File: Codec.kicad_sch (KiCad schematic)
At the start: 1 part, among them U5 TAC5242

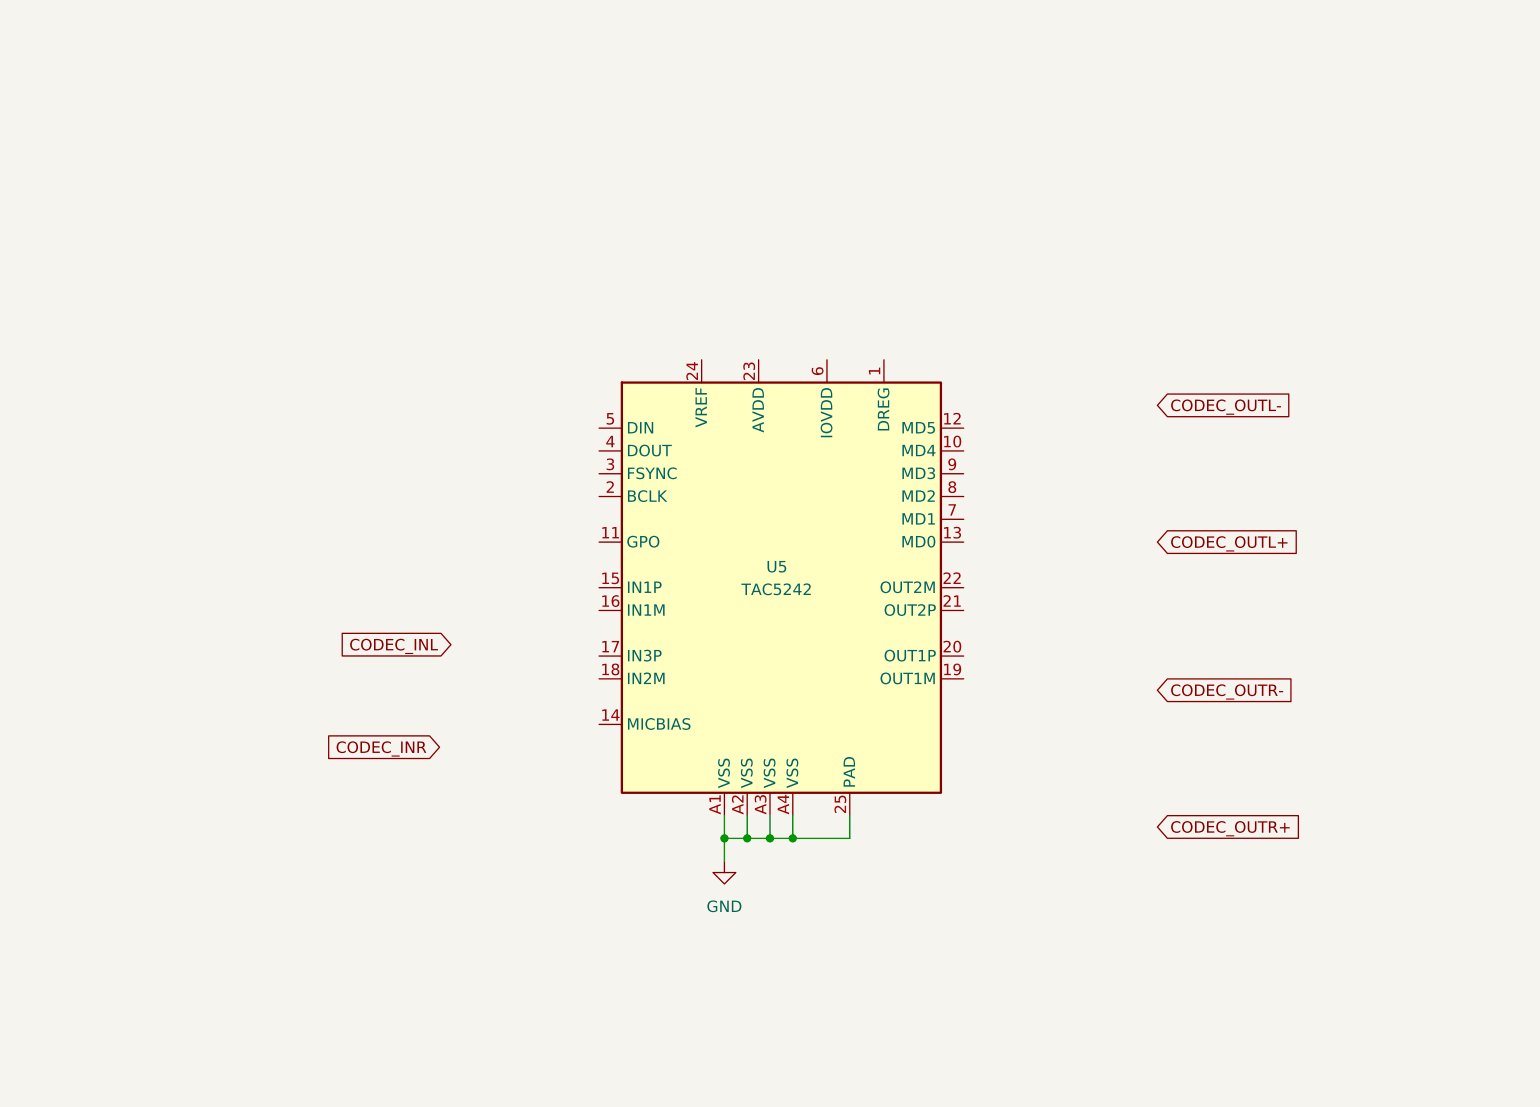
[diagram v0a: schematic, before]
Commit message: Schematic
Updated the schematic.
Added the codec schematic module.
Added the buffer schematic module.
Added the RP2350 schematic module.
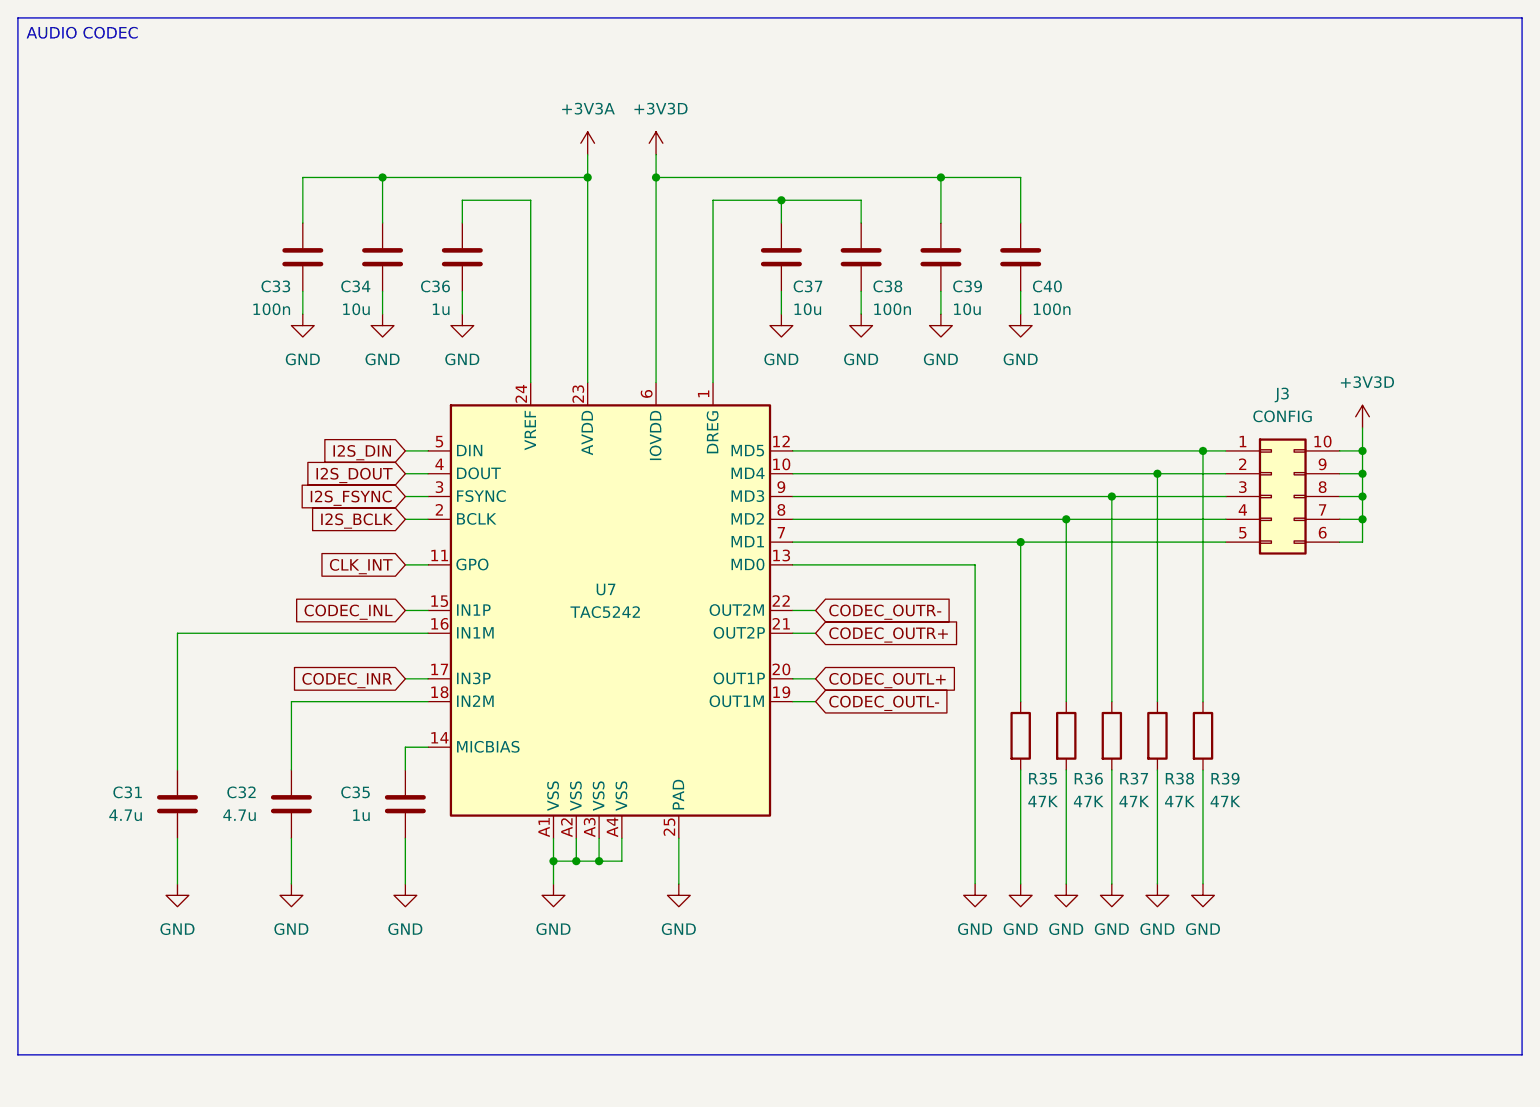
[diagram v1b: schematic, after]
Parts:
- added C31, C32: 4.7u, Capacitor_SMD:C_1206_3216Metric, symbol Device:C
- added C33, C38, C40: 100n, Capacitor_SMD:C_0603_1608Metric, symbol Device:C
- added C34, C37, C39: 10u, Capacitor_SMD:C_1206_3216Metric, symbol Device:C
- added C35, C36: 1u, Capacitor_SMD:C_0805_2012Metric, symbol Device:C
- added J3: CONFIG, Connector_PinHeader_1.27mm:PinHeader_2x05_P1.27mm_Vertical, symbol Connector_Generic:Conn_02x05_Counter_Clockwise
- added R35, R36, R37, R38, R39: 47K, Resistor_SMD:R_0603_1608Metric, symbol Device:R
- renumbered U5 to U7
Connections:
- net CODEC_INL: now also U7.15 (IN1P)
- net CODEC_INR: now also U7.17 (IN3P)
- net CODEC_OUTL+: now also U7.20 (OUT1P)
- net CODEC_OUTL-: now also U7.19 (OUT1M)
- net CODEC_OUTR+: now also U7.21 (OUT2P)
- net CODEC_OUTR-: now also U7.22 (OUT2M)
- net GND: now also U7.13 (MD0), C31.2, C32.2, C33.2, C34.2, C35.2, C36.2, C37.2, C38.2, C39.2, C40.2, R35.2, R36.2, R37.2, R38.2, R39.2
- net at U7.1 (DREG): now also C37.1, C38.1
- net at U7.10 (MD4): now also J3.2 (Pin_2), R38.1
- net CLK_INT: now reaches U7.11 (GPO)
- net at U7.12 (MD5): now also J3.1 (Pin_1), R39.1
- net at U7.14 (MICBIAS): now also C35.1
- net at U7.16 (IN1M): now also C31.1
- net at U7.18 (IN2M): now also C32.1
- net I2S_BCLK: now reaches U7.2 (BCLK)
- net +3V3A: now reaches U7.23 (AVDD)
- net +3V3A: now also C33.1, C34.1
- net at U7.24 (VREF): now also C36.1
- net I2S_FSYNC: now reaches U7.3 (FSYNC)
- net I2S_DOUT: now reaches U7.4 (DOUT)
- net I2S_DIN: now reaches U7.5 (DIN)
- net +3V3D: now reaches U7.6 (IOVDD)
- net +3V3D: now also C39.1, C40.1, J3.10 (Pin_10), J3.6 (Pin_6), J3.7 (Pin_7), J3.8 (Pin_8), J3.9 (Pin_9)
- net at U7.7 (MD1): now also J3.5 (Pin_5), R35.1
- net at U7.8 (MD2): now also J3.4 (Pin_4), R36.1
- net at U7.9 (MD3): now also J3.3 (Pin_3), R37.1
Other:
- moved on the sheet: U7

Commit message: Schematic
Updated the power delivery module.
Other minor changes.
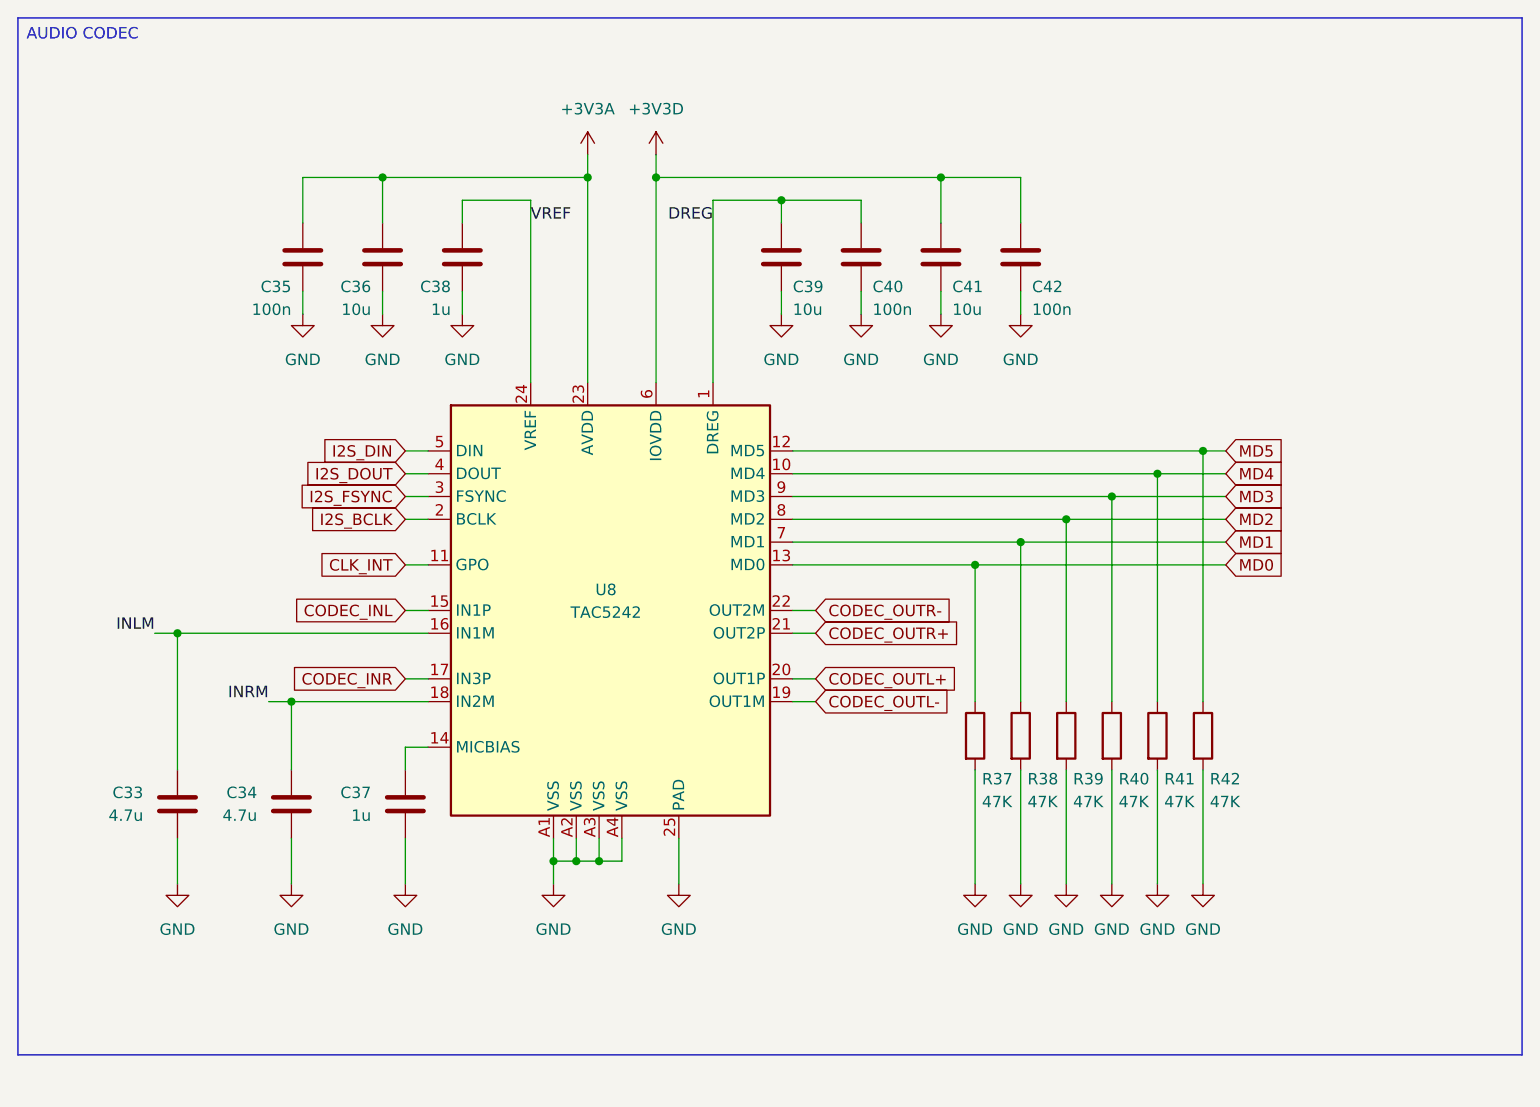
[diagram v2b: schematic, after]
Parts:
- removed J3: CONFIG, Connector_PinHeader_1.27mm:PinHeader_2x05_P1.27mm_Vertical, symbol Connector_Generic:Conn_02x05_Counter_Clockwise
- added R37: 47K, Resistor_SMD:R_0603_1608Metric, symbol Device:R
- renumbered C31 to C33, C32 to C34, C33 to C35, C34 to C36, C35 to C37, C36 to C38, C37 to C39, C38 to C40, C39 to C41, C40 to C42, R35 to R38, R36 to R39, R37 to R40, R38 to R41, R39 to R42, U7 to U8
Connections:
- net GND: now also R37.2; no longer U8.13 (MD0)
- net MD3: now reaches R40.1, U8.9 (MD3)
- net DREG: now reaches C39.1, C40.1, U8.1 (DREG)
- net MD4: now reaches R41.1, U8.10 (MD4)
- net MD5: now reaches R42.1, U8.12 (MD5)
- net INLM: now reaches C33.1, U8.16 (IN1M)
- net INRM: now reaches C34.1, U8.18 (IN2M)
- net VREF: now reaches C38.1, U8.24 (VREF)
- net MD1: now reaches R38.1, U8.7 (MD1)
- net MD2: now reaches R39.1, U8.8 (MD2)
- new net MD0: R37.1, U8.13 (MD0)
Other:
- company: (none) -> DavidMolTor
- title: (none) -> SIMPLE CODEC

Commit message: Moved to a CS4272 codec as a cheaper alternative with similar performance.
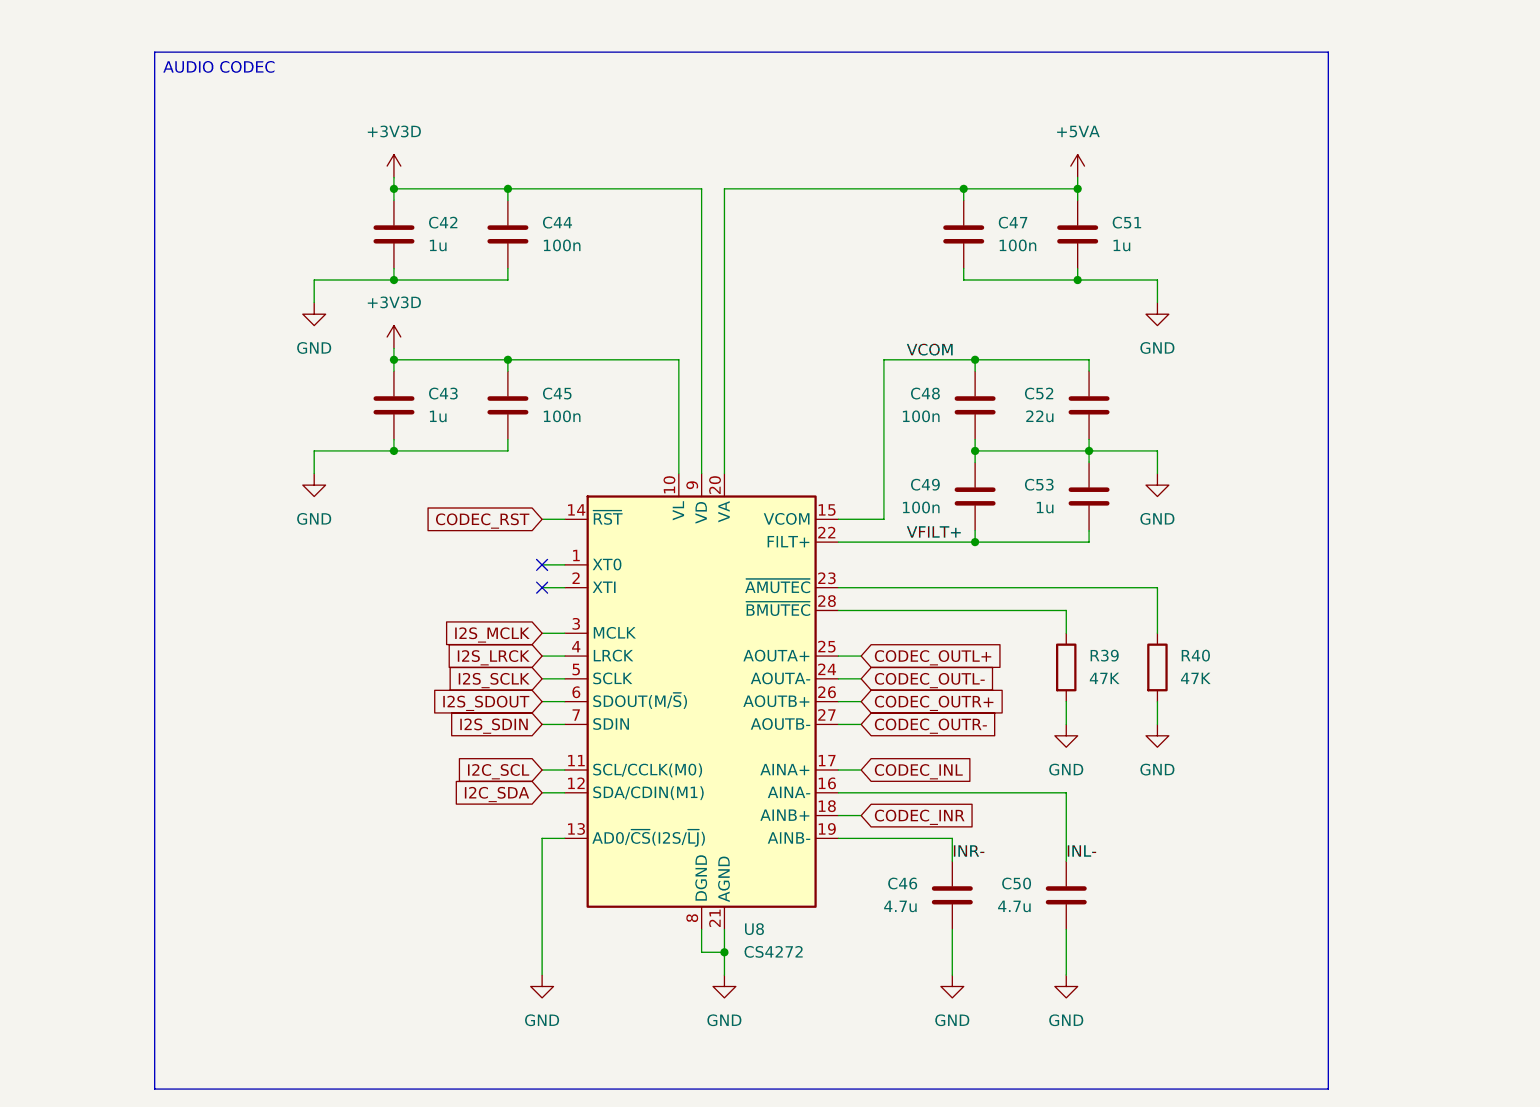
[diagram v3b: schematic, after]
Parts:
- removed C33, C34: 4.7u, Capacitor_SMD:C_1206_3216Metric, symbol Device:C
- removed C35, C40: 100n, Capacitor_SMD:C_0603_1608Metric, symbol Device:C
- removed C36, C39, C41: 10u, Capacitor_SMD:C_1206_3216Metric, symbol Device:C
- removed C37, C38: 1u, Capacitor_SMD:C_0805_2012Metric, symbol Device:C
- removed R37, R38, R41, R42: 47K, Resistor_SMD:R_0603_1608Metric, symbol Device:R
- removed U8: TAC5242, Custom_Parts:VQFN-24-1EP_4x4mm_P0.5mm_EP2.1x2.1mm_ThermalVias, symbol Custom_Parts:TAC5242
- added C43, C51, C53: 1u, Capacitor_SMD:C_0805_2012Metric, symbol Device:C
- added C44, C45, C47, C48, C49: 100n, Capacitor_SMD:C_0603_1608Metric, symbol Device:C
- added C46, C50: 4.7u, Capacitor_SMD:C_1206_3216Metric, symbol Device:C
- added C52: 22u, Capacitor_SMD:C_1206_3216Metric, symbol Device:C
- added U8: CS4272, Package_SO:TSSOP-28_4.4x9.7mm_P0.65mm, symbol Audio:CS4272
- C42: value 100n -> 1u; footprint Capacitor_SMD:C_0603_1608Metric -> Capacitor_SMD:C_0805_2012Metric
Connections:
- net +3V3D: now also C42.2, C43.2, C44.1, C45.1, U8.10 (VL), U8.9 (VD); no longer C42.1
- net CODEC_INL: now also U8.17 (AINA+)
- net CODEC_INR: now also U8.18 (AINB+)
- net CODEC_OUTL+: now also U8.25 (AOUTA+)
- net CODEC_OUTL-: now also U8.24 (AOUTA-)
- net CODEC_OUTR+: now also U8.26 (AOUTB+)
- net CODEC_OUTR-: now also U8.27 (AOUTB-)
- net GND: now also C42.1, C43.1, C44.2, C45.2, C46.2, C47.1, C48.2, C49.2, C50.2, C51.2, C52.2, C53.1, U8.13 (AD0/~{CS}(I2S/~{LJ})), U8.21 (AGND), U8.8 (DGND); no longer C42.2
- net MD2: no longer names the net of R39.1
- net MD2: now also U8.28 (~{BMUTEC})
- net MD3: no longer names the net of R40.1
- net MD3: now also U8.23 (~{AMUTEC})
- new net +5VA: C47.2, C51.1, U8.20 (VA)
- new net CODEC_RST: U8.14 (~{RST})
- new net I2C_SCL: U8.11 (SCL/CCLK(M0))
- new net I2C_SDA: U8.12 (SDA/CDIN(M1))
- new net I2S_LRCK: U8.4 (LRCK)
- new net I2S_MCLK: U8.3 (MCLK)
- new net I2S_SCLK: U8.5 (SCLK)
- new net I2S_SDIN: U8.7 (SDIN)
- new net I2S_SDOUT: U8.6 (SDOUT(M/~{S}))
- new net INL-: C50.1, U8.16 (AINA-)
- new net INR-: C46.1, U8.19 (AINB-)
- new net VCOM: C48.1, C52.1, U8.15 (VCOM)
- new net VFILT+: C49.1, C53.2, U8.22 (FILT+)
- no-connect marks 0 -> 2

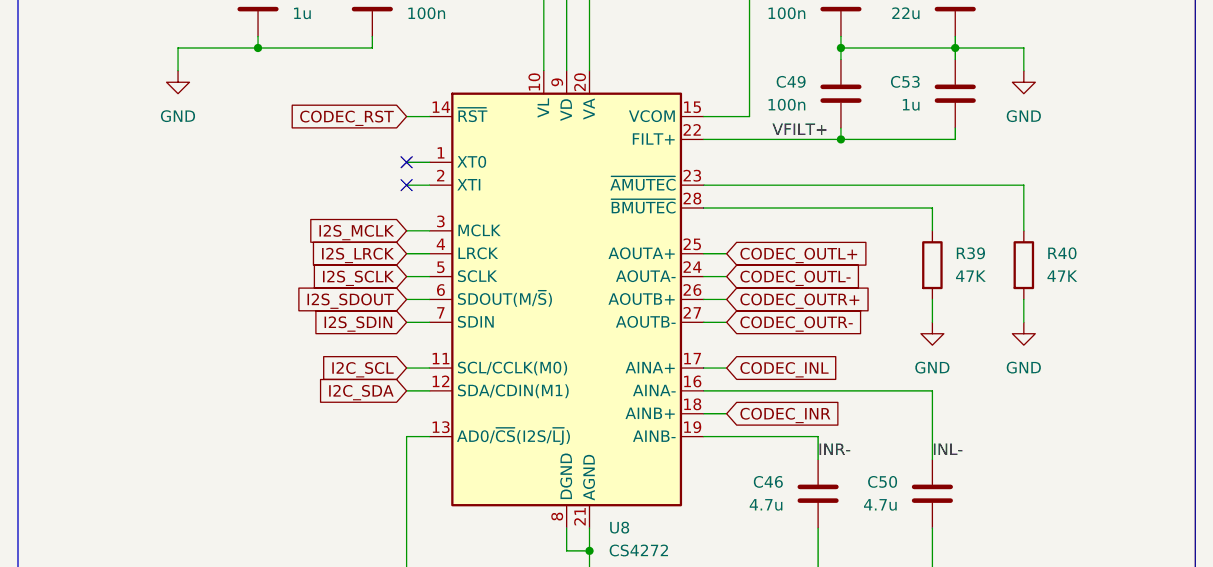
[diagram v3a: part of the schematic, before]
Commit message: Initial layout
Initial layout inside a 1590N1/125B pedal enclosure.
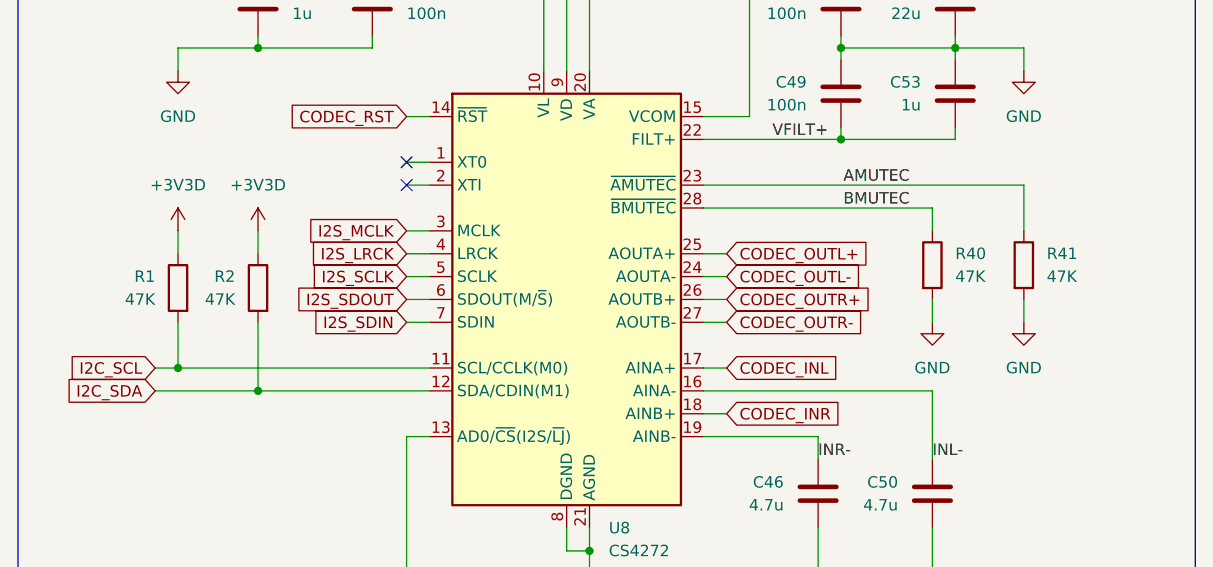
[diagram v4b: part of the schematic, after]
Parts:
- added R1, R2: 47K, Resistor_SMD:R_0603_1608Metric, symbol Device:R
- renumbered R39 to R40, R40 to R41
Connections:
- net +3V3D: now also R1.1, R2.1
- net I2C_SCL: now also R1.2
- net I2C_SDA: now also R2.2
- net AMUTEC: now reaches R41.1, U8.23 (~{AMUTEC})
- net BMUTEC: now reaches R40.1, U8.28 (~{BMUTEC})
